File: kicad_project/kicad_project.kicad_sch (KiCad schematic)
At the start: 3 parts, among them U1 RP2040

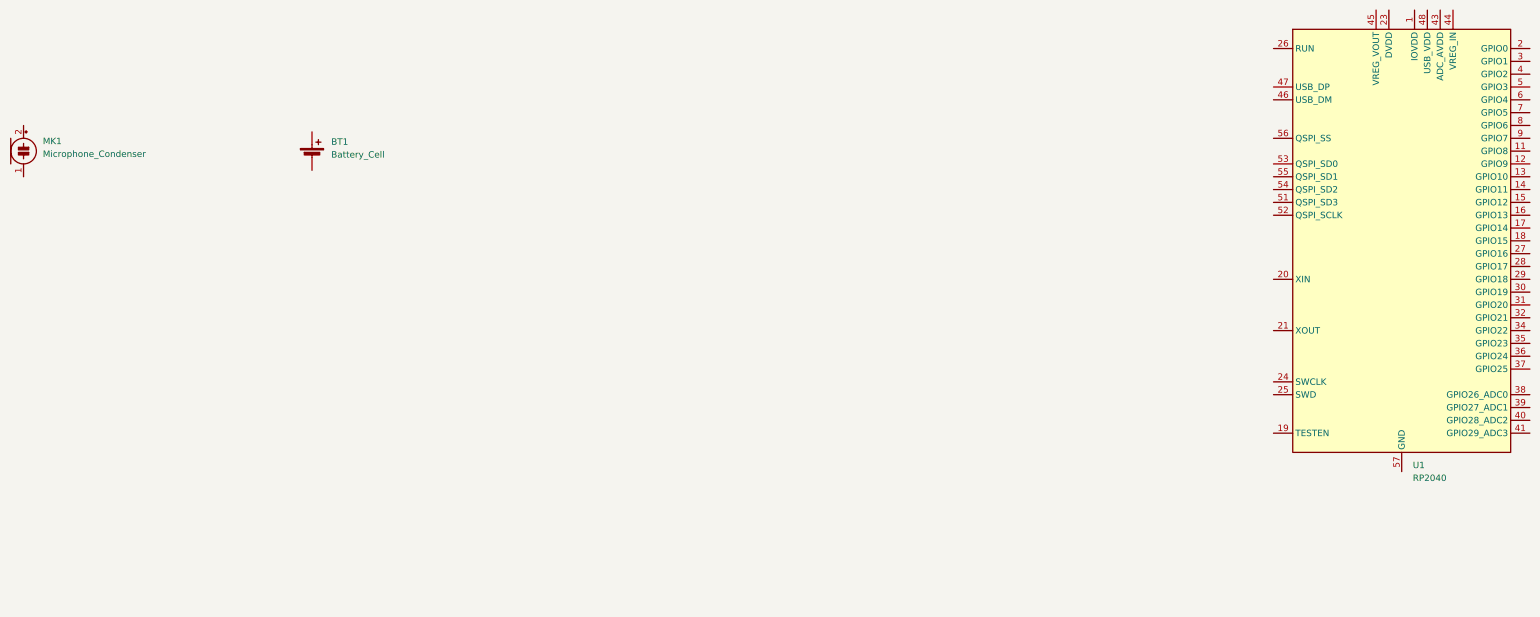
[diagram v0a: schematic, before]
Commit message: KiCAD Additions of the Data Buses. Implemented FFT, graphing of it (NOT TESTED). Implemented audio input and output.
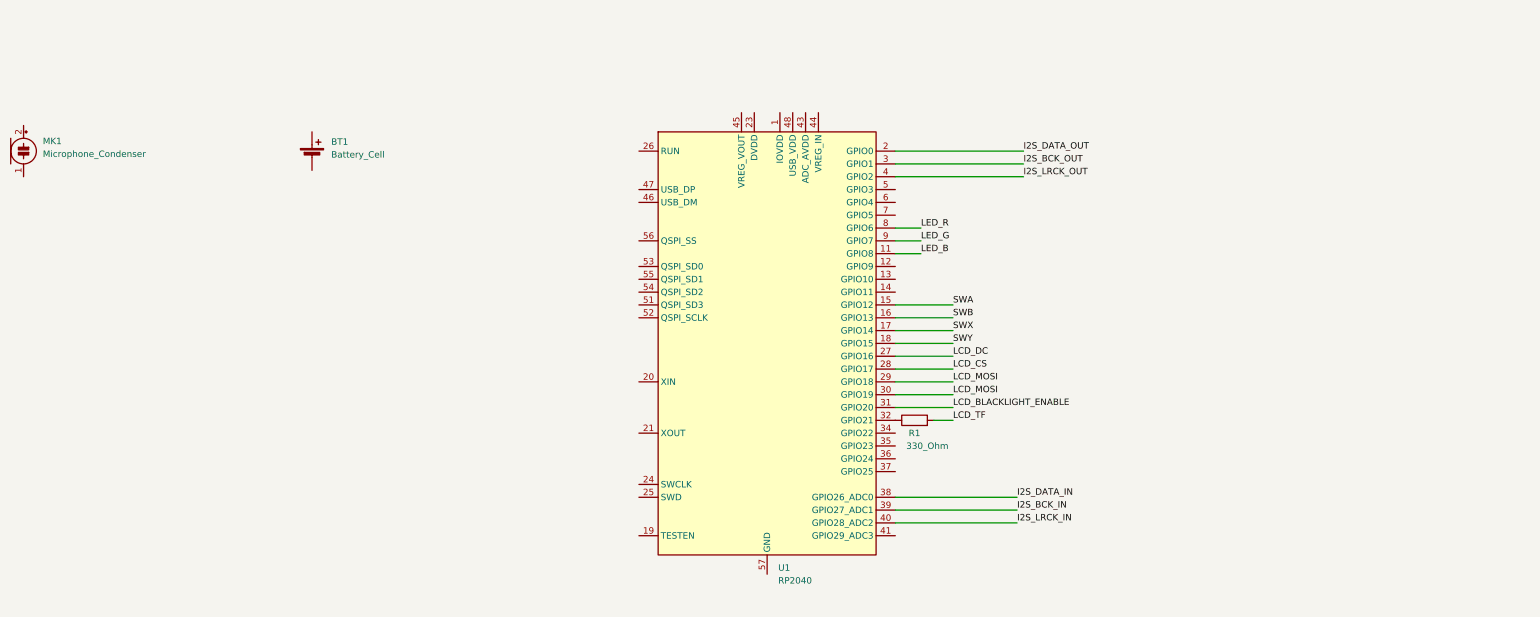
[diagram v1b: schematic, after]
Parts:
- added R1: 330_Ohm, symbol Device:R
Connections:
- net LED_B: now reaches U1.11 (GPIO8)
- net SWA: now reaches U1.15 (GPIO12)
- net SWB: now reaches U1.16 (GPIO13)
- net SWX: now reaches U1.17 (GPIO14)
- net SWY: now reaches U1.18 (GPIO15)
- net I2S_DATA_OUT: now reaches U1.2 (GPIO0)
- net LCD_DC: now reaches U1.27 (GPIO16)
- net LCD_CS: now reaches U1.28 (GPIO17)
- net LCD_MOSI: now reaches U1.29 (GPIO18)
- net LCD_MOSI: now also U1.30 (GPIO19)
- net I2S_BCK_OUT: now reaches U1.3 (GPIO1)
- net LCD_BLACKLIGHT_ENABLE: now reaches U1.31 (GPIO20)
- net at U1.32 (GPIO21): now also R1.1
- net I2S_DATA_IN: now reaches U1.38 (GPIO26_ADC0)
- net I2S_BCK_IN: now reaches U1.39 (GPIO27_ADC1)
- net I2S_LRCK_OUT: now reaches U1.4 (GPIO2)
- net I2S_LRCK_IN: now reaches U1.40 (GPIO28_ADC2)
- net LED_R: now reaches U1.8 (GPIO6)
- net LED_G: now reaches U1.9 (GPIO7)
- new net LCD_TF: R1.2
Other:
- moved on the sheet: U1

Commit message: Updated KiCAD and played around with the code.
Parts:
- added R2, R3: 1.3kOhm, symbol Device:R
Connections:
- net SPI1 CSn: now reaches U1.12 (GPIO9)
- net SPI CLK: now reaches U1.13 (GPIO10)
- net SPI1 TX: now reaches U1.14 (GPIO11)
- net Vcc: now reaches U1.44 (VREG_IN)
- net Vcc: now also R2.2, R3.2
- net GND: now reaches U1.57 (GND)
- net I2C0_SDA: now reaches U1.6 (GPIO4)
- net I2C0_SDA: now also R2.1
- net I2C0_SCL: now reaches U1.7 (GPIO5)
- net I2C0_SCL: now also R3.1
- net LED_B renamed SPI1 RX
- net LED_G: no longer names the net of U1.9 (GPIO7)
- net LED_R: no longer names the net of U1.8 (GPIO6)
